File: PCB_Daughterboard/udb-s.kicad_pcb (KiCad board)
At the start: 2 copper layers, 49.5 x 20.6 mm, 10 parts, among them J1 TYPE-C-31-M-12, J2 78171-0004, U1 TPD4E05U06DQAR

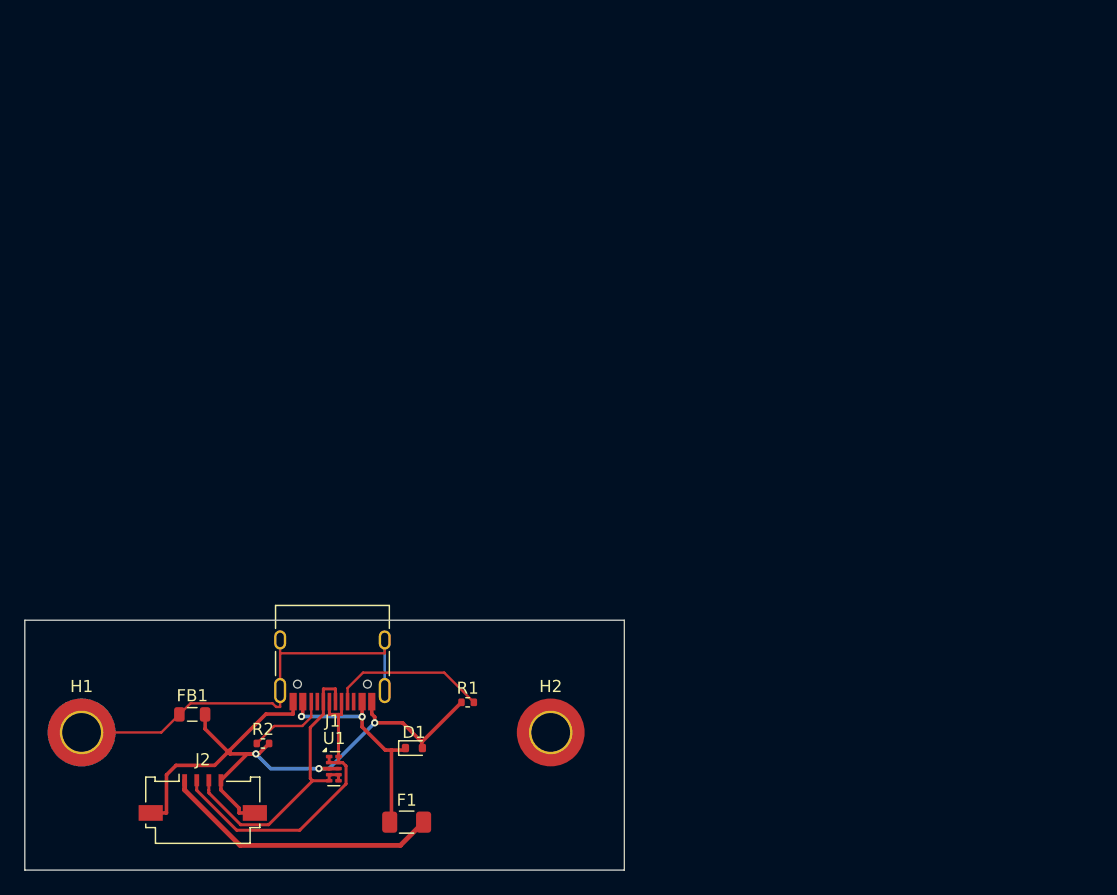
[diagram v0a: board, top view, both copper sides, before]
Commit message: Update daughterboard to adapt keyboard
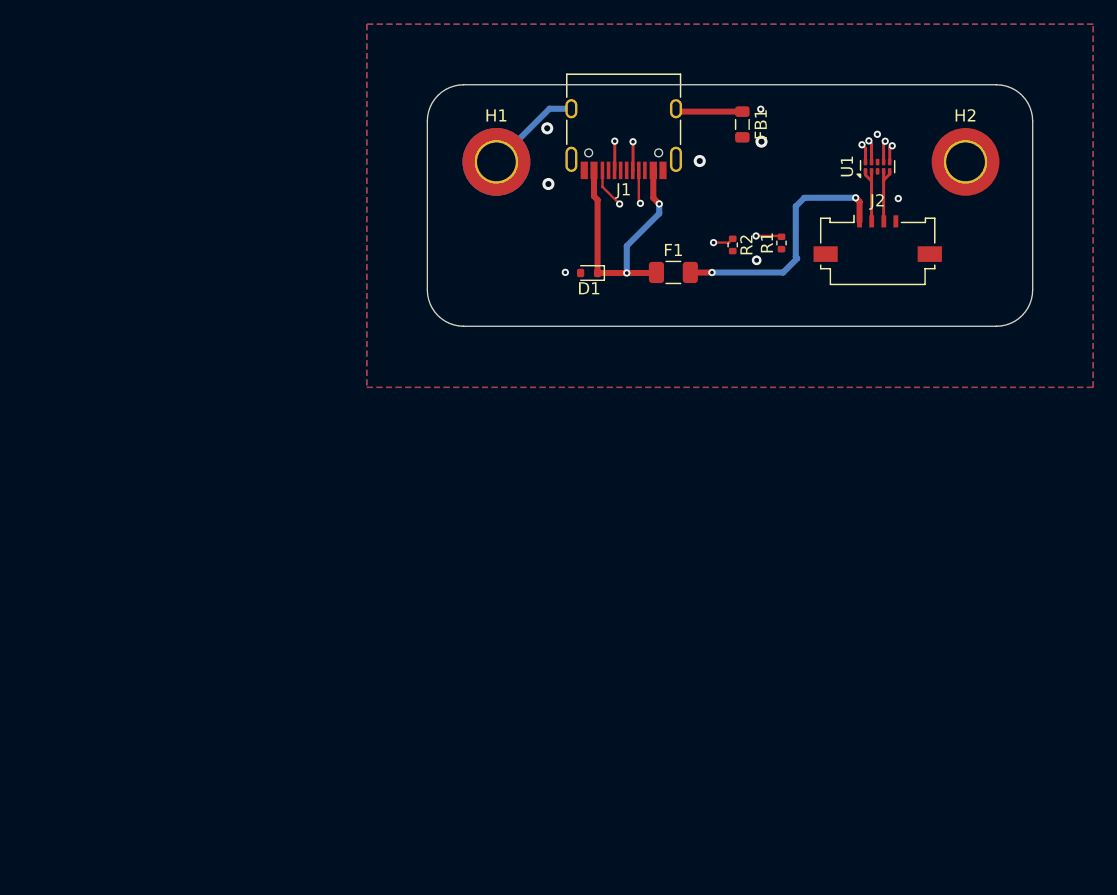
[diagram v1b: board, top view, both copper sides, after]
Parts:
- moved J2 72.4 mm to (170.7, 43.7)
- moved U1 67.0 mm to (170.7, 38.3), turned to 90 degrees
- moved FB1 66.6 mm to (159.5, 34.8), turned to -90 degrees
- moved H1 58.3 mm to (139.2, 37.9)
- moved H2 58.3 mm to (178.0, 37.9)
- moved R2 56.6 mm to (158.7, 44.7), turned to -90 degrees
- moved F1 50.5 mm to (153.8, 47.0)
- moved J1 50.0 mm to (149.7, 34.5)
- moved R1 45.9 mm to (162.8, 44.6), turned to 90 degrees
- moved D1 41.8 mm to (146.9, 47.0), turned to 180 degrees
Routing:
- net GND: track 59.5 -> 0.00 mm, vias 3 -> 8
- net D+: track 25.5 -> 61.2 mm, vias 0 -> 3
- net D-: track 26.7 -> 52.7 mm, vias 0 -> 3
- net GNDPWR: track 37.0 -> 11.3 mm
- net Net-(J1-CC2): track 6.68 -> 14.2 mm, vias 0 -> 2
- net VBUS: track 18.8 -> 23.3 mm
- net Net-(J1-CC1): track 13.1 -> 15.6 mm, vias 0 -> 2
- net 5V: track 23.2 -> 21.0 mm, vias 0 -> 2
- net (no net): vias 0 -> 1
- added copper zone on B.Cu, net D+
- added copper zone on F.Cu, net GND
- added copper zone on In1.Cu, net GND
- added copper zone on In2.Cu, net GND
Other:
- board size 49.5 x 20.6 mm -> 50 x 20 mm
- copper layers 2 -> 4
